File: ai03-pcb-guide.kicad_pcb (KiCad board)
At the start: 2 copper layers, 24 parts, among them SW1 SW_Push, U1 ATmega32U4-AU, Y1 16MHz

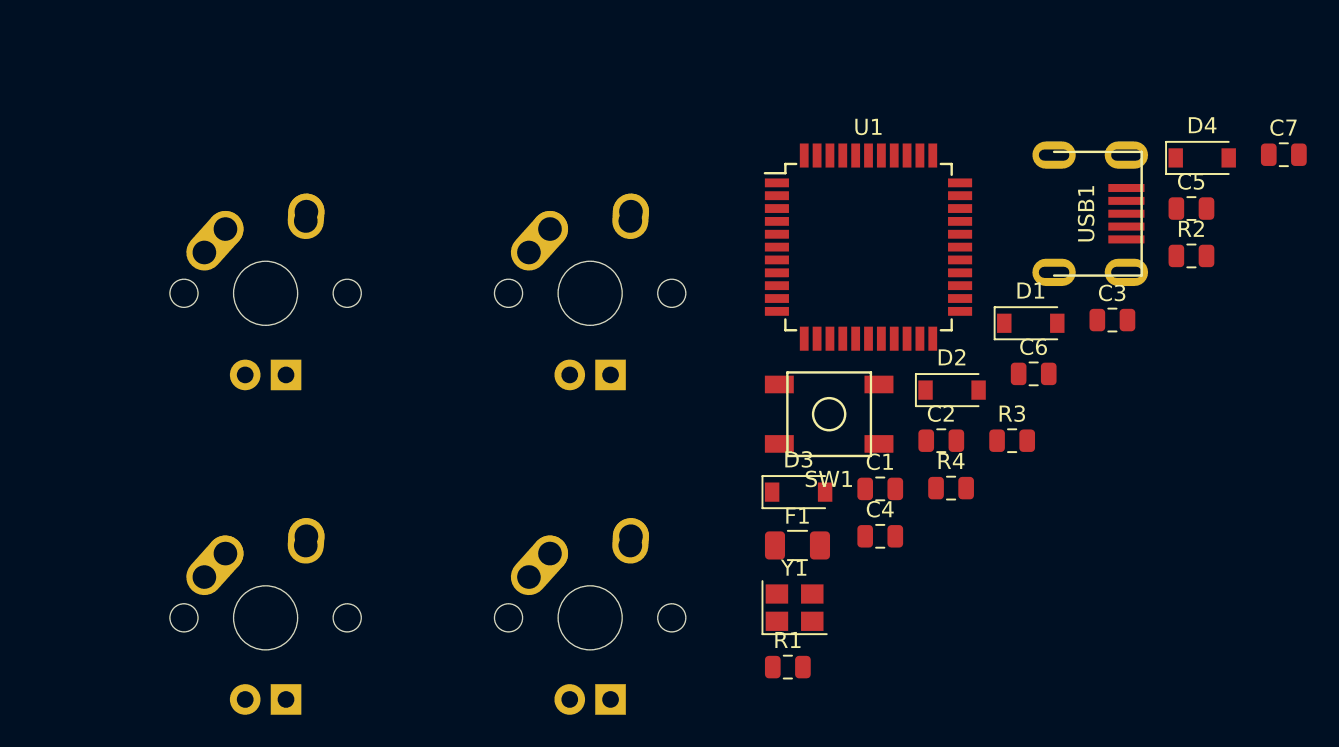
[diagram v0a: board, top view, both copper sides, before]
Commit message: reorganize switches in correct order
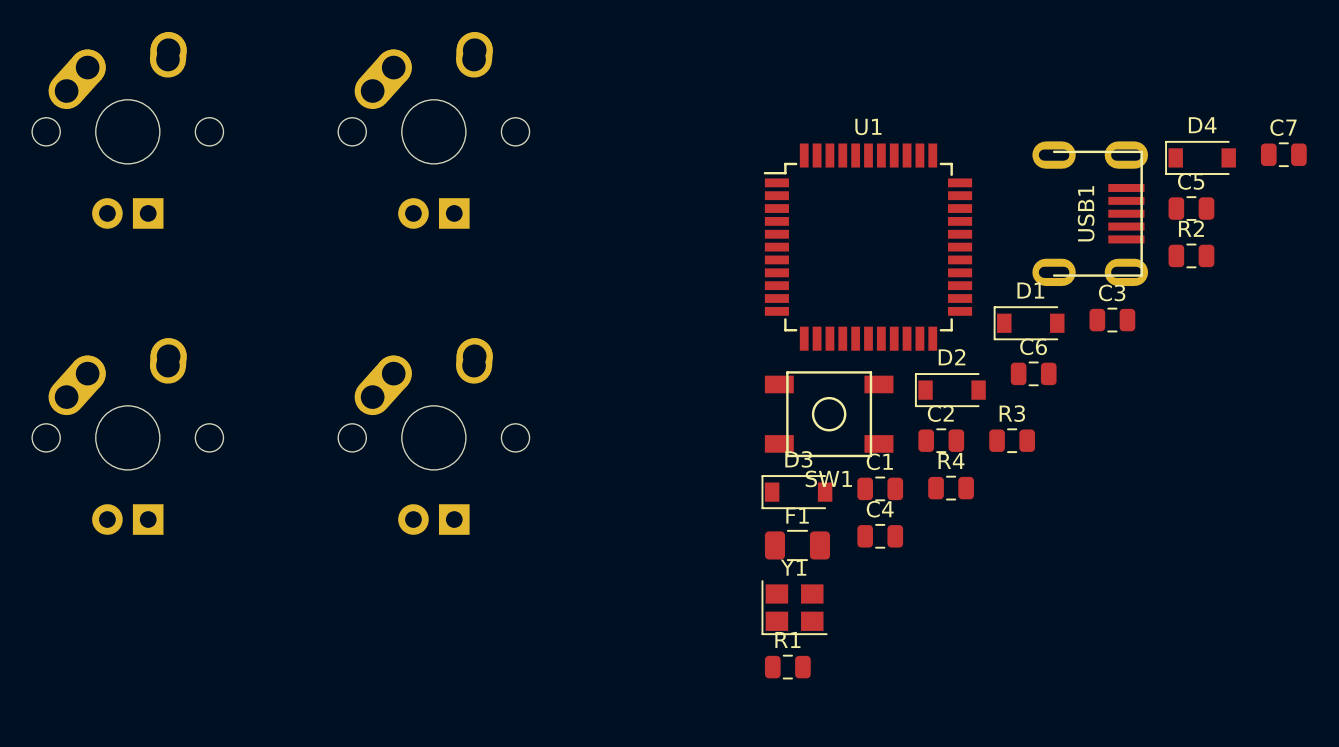
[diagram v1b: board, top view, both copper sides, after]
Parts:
- moved MX2 32.0 mm to (133.3, 77.0)
- moved MX3 30.2 mm to (114.3, 96.0)
- moved MX4 14.8 mm to (133.3, 96.0)
- moved MX1 13.2 mm to (114.3, 77.0)
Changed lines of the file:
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@@
   )
   (module MX_Alps_Hybrid:MX-1U (layer F.Cu)
-    (at 143.07625 107.24375)
+    (at 133.35 96.04375)
     (fp_text reference MX4 (at 0 3.175) (layer Dwgs.User)
       (effects (font (size 1 1) (thickness 0.15)))
@@
   )
   (module MX_Alps_Hybrid:MX-1U (layer F.Cu)
-    (at 143.07625 87.04375)
+    (at 114.3 96.04375)
     (fp_text reference MX3 (at 0 3.175) (layer Dwgs.User)
       (effects (font (size 1 1) (thickness 0.15)))
@@
   )
   (module MX_Alps_Hybrid:MX-1U (layer F.Cu)
-    (at 122.87625 107.24375)
+    (at 133.35 76.99375)
     (fp_text reference MX2 (at 0 3.175) (layer Dwgs.User)
       (effects (font (size 1 1) (thickness 0.15)))
@@
   )
   (module MX_Alps_Hybrid:MX-1U (layer F.Cu)
-    (at 122.87625 87.04375)
+    (at 114.3 76.99375)
     (fp_text reference MX1 (at 0 3.175) (layer Dwgs.User)
       (effects (font (size 1 1) (thickness 0.15)))
